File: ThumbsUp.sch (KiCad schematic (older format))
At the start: 159 parts, among them J19 52559-1233, J32 Battery, SW1 SW_Push, SW2 SW_DIP_x01, U1 ProMicro

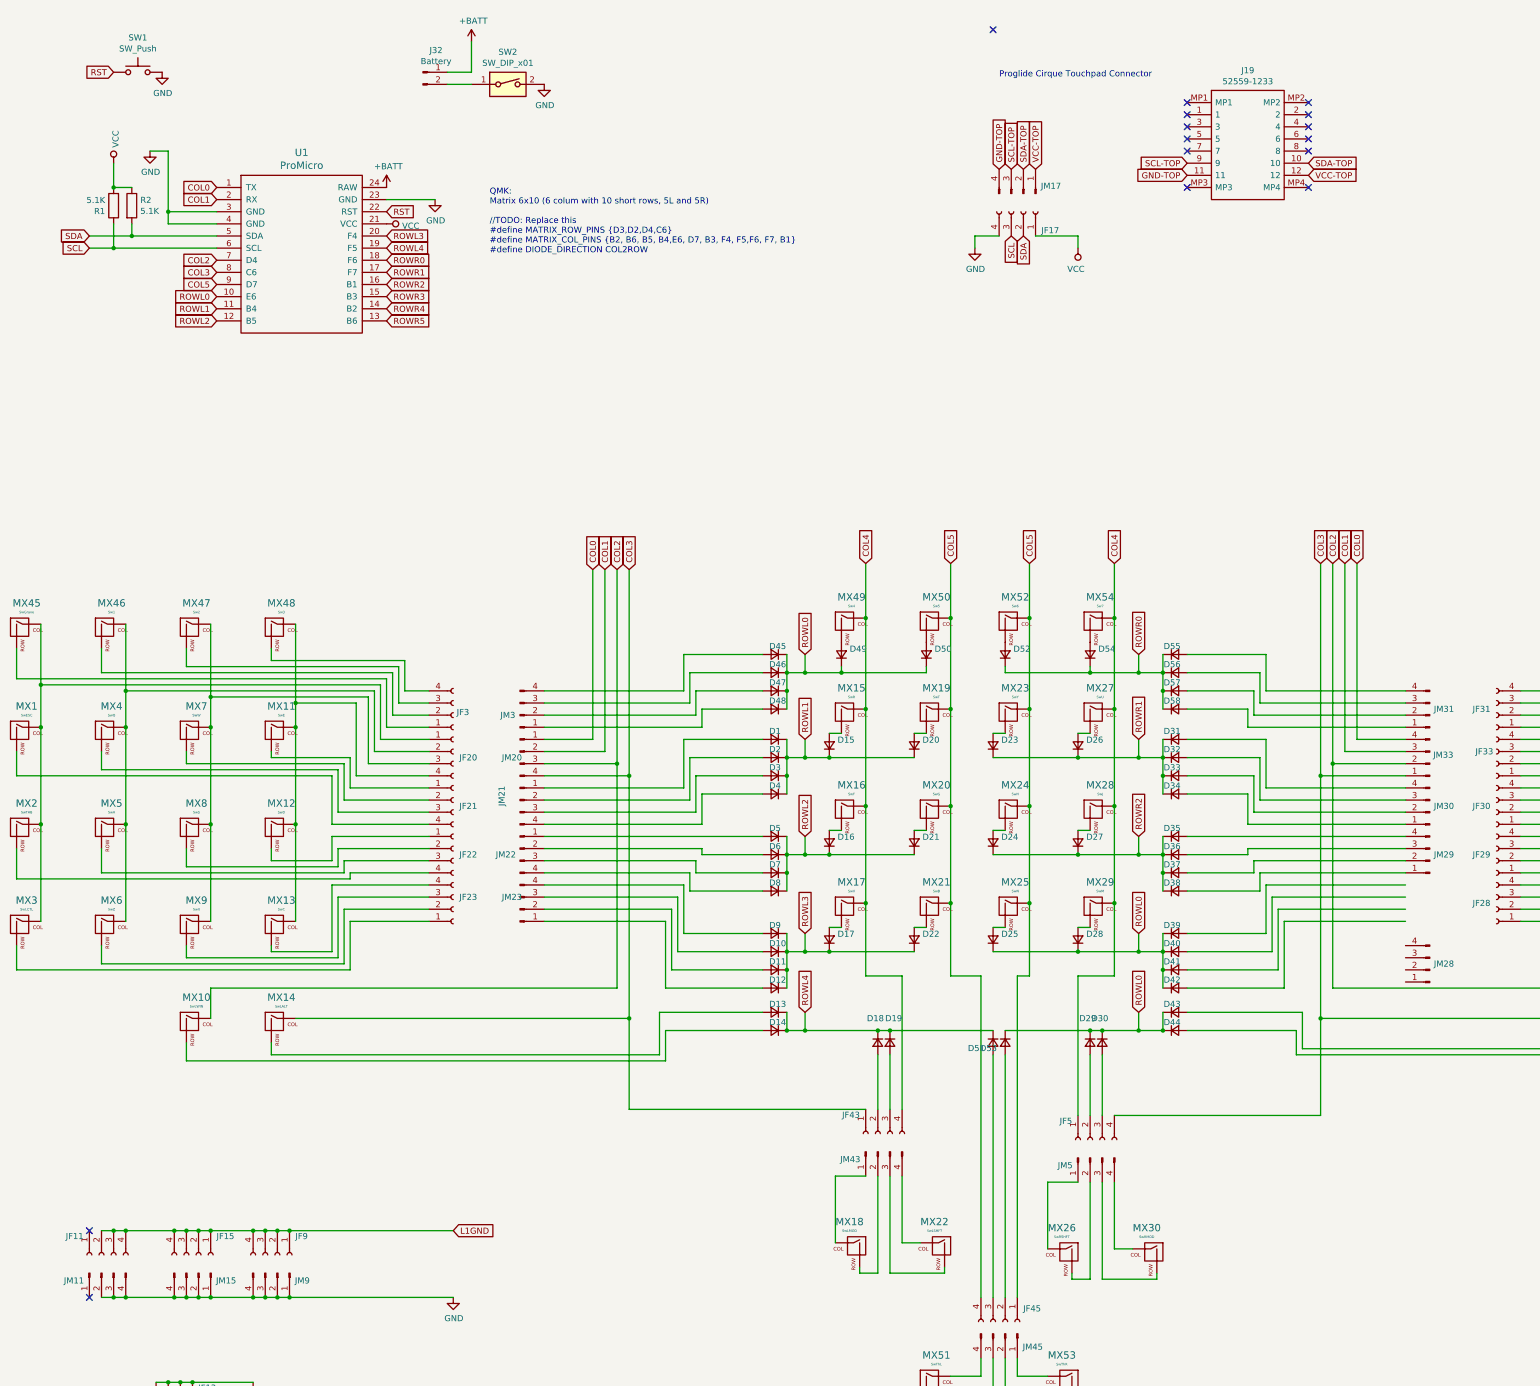
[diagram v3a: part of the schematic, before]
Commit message: Routed L2 PCB
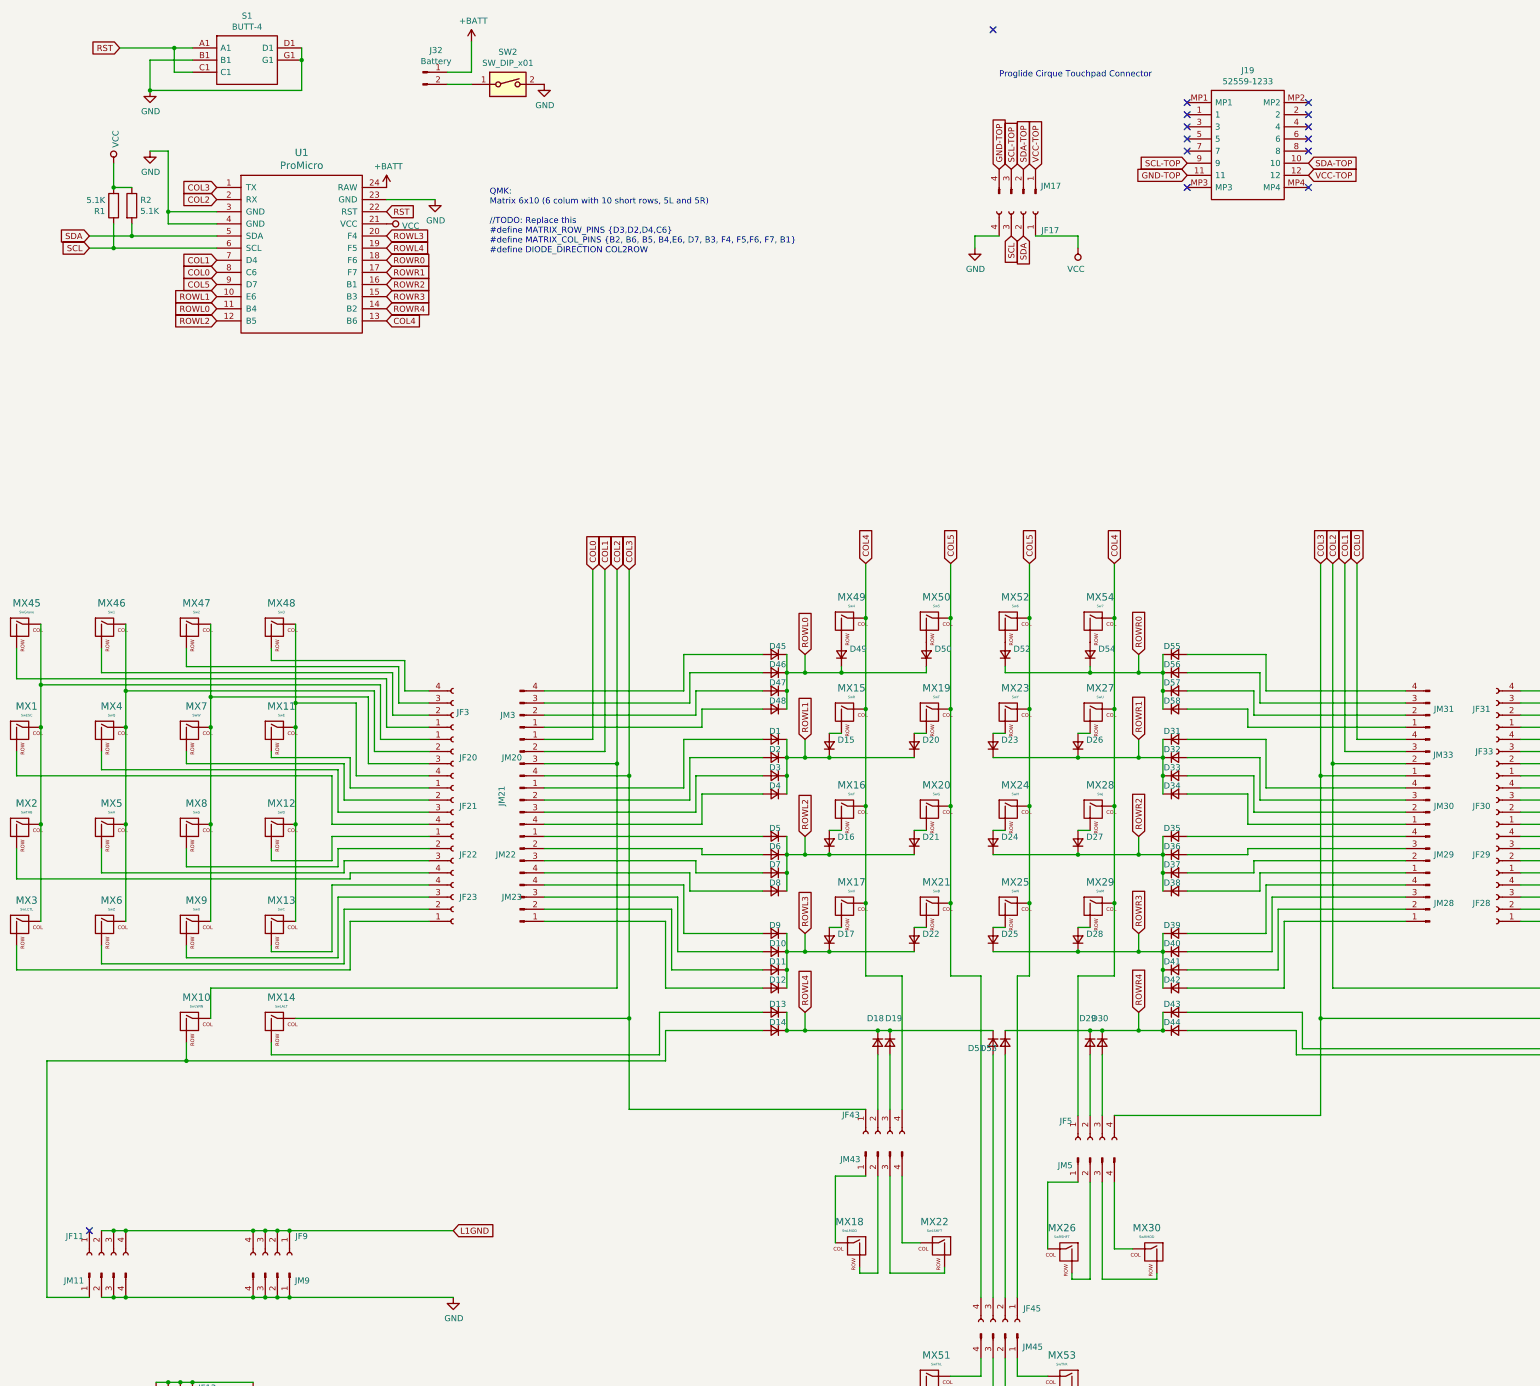
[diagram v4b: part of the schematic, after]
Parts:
- removed JF15: Raiser_Female, Connector_PinSocket_2.54mm:PinSocket_1x04_P2.54mm_Vertical, symbol Connector:Conn_01x04_Female
- removed JM15: Raiser_Male, Connector_PinHeader_2.54mm:PinHeader_1x04_P2.54mm_Vertical, symbol Connector:Conn_01x04_Male
- removed SW1: SW_Push, random-keyboard-parts:SKQG-1155865, symbol Switch:SW_Push
- added S1: BUTT-4, BUTT-4:BUTT4, symbol BUTT-4:BUTT-4
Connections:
- net ROWR5 is gone; now on net COL4: U1.13 (B6)
- net COL0: now also U1.8 (C6); no longer U1.1 (TX)
- net COL1: now also U1.7 (D4); no longer U1.2 (RX)
- net COL2: now also U1.2 (RX); no longer U1.7 (D4)
- net COL3: now also U1.1 (TX); no longer U1.8 (C6)
- net GND: now also S1.B1, S1.D1, S1.G1
- net ROWL0: now also U1.11 (B4); no longer D25.1 (K), D28.1 (K), D29.1 (K), D30.1 (K), D39.1 (K), D40.1 (K), D41.1 (K), D42.1 (K), D43.1 (K), D44.1 (K), D53.1 (K), U1.10 (E6)
- net ROWL1: now also U1.10 (E6); no longer U1.11 (B4)
- net ROWR3: now also D25.1 (K), D28.1 (K), D39.1 (K), D40.1 (K), D41.1 (K), D42.1 (K)
- net ROWR4: now also D29.1 (K), D30.1 (K), D43.1 (K), D44.1 (K), D53.1 (K)
- net RST: now also S1.A1, S1.C1
- net at D14.2 (A), MX10.2 (ROW): now also JM11.1 (Pin_1)
- net at D39.2 (A): now also JM28.4 (Pin_4)
- net at D40.2 (A): now also JM28.3 (Pin_3)
- net at D41.2 (A): now also JM28.2 (Pin_2)
- net at D42.2 (A): now also JM28.1 (Pin_1)
- no-connect marks 15 -> 14
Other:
- moved on the sheet: JM28
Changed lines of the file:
@@
-$EndComp
-$Comp
-L Connector:Conn_01x04_Female JF15
-U 1 1 6225ECEC
-P 2750 11050
-F 0 "JF15" V 2596 11198 50  0000 L CNN
-F 1 "Raiser_Female" V 2687 11198 50  0001 L CNN
-F 2 "Connector_PinSocket_2.54mm:PinSocket_1x04_P2.54mm_Vertical" H 2750 11050 50  0001 C CNN
-F 3 "~" H 2750 11050 50  0001 C CNN
-	1    2750 11050
-	0    1    1    0
-$EndComp
-$Comp
-L Connector:Conn_01x04_Male JM15
-U 1 1 6225ECF6
-P 2750 11200
-F 0 "JM15" V 2812 11344 50  0000 L CNN
-F 1 "Raiser_Male" V 2903 11344 50  0001 L CNN
-F 2 "Connector_PinHeader_2.54mm:PinHeader_1x04_P2.54mm_Vertical" H 2750 11200 50  0001 C CNN
-F 3 "~" H 2750 11200 50  0001 C CNN
-	1    2750 11200
-	0    1    1    0
 $EndComp
 $Comp
@@
 Text GLabel 1850 2750 0    50   Input ~ 0
 SCL
+Text GLabel 2900 2950 0    50   Input ~ 0
+COL0
+Text GLabel 2900 2850 0    50   Input ~ 0
+COL1
+Text GLabel 2900 2350 0    50   Input ~ 0
+COL2
 Text GLabel 2900 2250 0    50   Input ~ 0
-COL0
-Text GLabel 2900 2350 0    50   Input ~ 0
-COL1
-Text GLabel 2900 2850 0    50   Input ~ 0
-COL2
-Text GLabel 2900 2950 0    50   Input ~ 0
 COL3
 Text GLabel 2900 3050 0    50   Input ~ 0
 COL5
+Text GLabel 2900 3250 0    50   Input ~ 0
+ROWL0
 Text GLabel 2900 3150 0    50   Input ~ 0
-ROWL0
-Text GLabel 2900 3250 0    50   Input ~ 0
 ROWL1
 Text GLabel 2900 3350 0    50   Input ~ 0
@@
 Text GLabel 4300 3050 2    50   Input ~ 0
 ROWR2
-Text GLabel 4300 2950 2    50   Input ~ 0
-ROWR1
-Text GLabel 4300 2850 2    50   Input ~ 0
-ROWR0
 Text GLabel 4300 2750 2    50   Input ~ 0
 ROWL4
@@
 Text GLabel 4300 2450 2    50   Input ~ 0
 RST
-$Comp
-L Switch:SW_Push SW1
-U 1 1 63887BED
-P 2250 1300
-F 0 "SW1" H 2250 1585 50  0000 C CNN
-F 1 "SW_Push" H 2250 1494 50  0000 C CNN
-F 2 "random-keyboard-parts:SKQG-1155865" H 2250 1500 50  0001 C CNN
-F 3 "~" H 2250 1500 50  0001 C CNN
-	1    2250 1300
-	1    0    0    -1
-$EndComp
-Text GLabel 2050 1300 0    50   Input ~ 0
+Text GLabel 2100 1100 0    50   Input ~ 0
 RST
 $Comp
 L power:GND #PWR0104
 U 1 1 6388A683
-P 2450 1300
-F 0 "#PWR0104" H 2450 1050 50  0001 C CNN
-F 1 "GND" H 2455 1127 50  0000 C CNN
-F 2 "" H 2450 1300 50  0001 C CNN
-F 3 "" H 2450 1300 50  0001 C CNN
-	1    2450 1300
+P 2350 1450
+F 0 "#PWR0104" H 2350 1200 50  0001 C CNN
+F 1 "GND" H 2355 1277 50  0000 C CNN
+F 2 "" H 2350 1450 50  0001 C CNN
+F 3 "" H 2350 1450 50  0001 C CNN
+	1    2350 1450
 	1    0    0    -1
 $EndComp
@@
 $EndComp
 Text GLabel 10500 9050 1    50   Input ~ 0
-ROWL0
+ROWR4
 Text GLabel 10500 8400 1    50   Input ~ 0
-ROWL0
+ROWR3
 Wire Wire Line
 	9400 9400 9400 11400
@@
 Text GLabel 4300 3250 2    50   Input ~ 0
 ROWR4
-Text GLabel 4300 3350 2    50   Input ~ 0
-ROWR5
 Text GLabel 4300 3150 2    50   Input ~ 0
 ROWR3
@@
 	0    1    1    0
 $EndComp
-Connection ~ 2550 10850
-Wire Wire Line
-	2550 10850 2650 10850
-Connection ~ 2650 10850
-Wire Wire Line
-	2650 10850 2750 10850
-Connection ~ 2750 10850
-Wire Wire Line
-	2750 10850 2850 10850
-Connection ~ 2850 10850
-Wire Wire Line
-	2850 10850 3200 10850
 Connection ~ 3200 10850
 Wire Wire Line
@@
 	3400 10850 3500 10850
 Connection ~ 3500 10850
-Connection ~ 2550 11400
-Wire Wire Line
-	2550 11400 2650 11400
-Connection ~ 2650 11400
-Wire Wire Line
-	2650 11400 2750 11400
-Connection ~ 2750 11400
-Wire Wire Line
-	2750 11400 2850 11400
-Connection ~ 2850 11400
-Wire Wire Line
-	2850 11400 3200 11400
 Connection ~ 3200 11400
 Wire Wire Line
@@
 	9650 2650 10000 2650
 Wire Wire Line
-	2150 10850 2550 10850
-Wire Wire Line
 	1950 10850 2050 10850
 Connection ~ 2150 10850
@@
 NoConn ~ 1850 10850
 Wire Wire Line
-	2150 11400 2550 11400
-Wire Wire Line
 	2150 11400 2050 11400
 Connection ~ 2150 11400
@@
 Wire Wire Line
 	2050 11400 1950 11400
-NoConn ~ 1850 11400
 $Comp
 L Connector:Conn_01x04_Female JF31
@@
 L Connector:Conn_01x04_Male JM28
 U 1 1 636DA3EC
-P 12900 8700
-F 0 "JM28" H 12700 8650 50  0000 L CNN
-F 1 "Conn_01x04_Male" H 13053 8844 50  0001 L CNN
-F 2 "Connector_PinHeader_2.54mm:PinHeader_1x04_P2.54mm_Vertical" H 12900 8700 50  0001 C CNN
-F 3 "~" H 12900 8700 50  0001 C CNN
-	1    12900 8700
+P 12900 8200
+F 0 "JM28" H 12700 8150 50  0000 L CNN
+F 1 "Conn_01x04_Male" H 13053 8344 50  0001 L CNN
+F 2 "Connector_PinHeader_2.54mm:PinHeader_1x04_P2.54mm_Vertical" H 12900 8200 50  0001 C CNN
+F 3 "~" H 12900 8200 50  0001 C CNN
+	1    12900 8200
 	-1   0    0    1
 $EndComp
@@
 L1GND
 $Comp
-L power:GND #PWR?
+L power:GND #PWR0112
 U 1 1 6569DA14
 P 3200 12100
-F 0 "#PWR?" H 3200 11850 50  0001 C CNN
+F 0 "#PWR0112" H 3200 11850 50  0001 C CNN
 F 1 "GND" H 3205 11927 50  0000 C CNN
 F 2 "" H 3200 12100 50  0001 C CNN
@@
 Wire Wire Line
 	2700 12600 3200 12600
+$Comp
+L BUTT-4:BUTT-4 S1
+U 1 1 646FD412
+P 2700 1100
+F 0 "S1" H 3150 1365 50  0000 C CNN
+F 1 "BUTT-4" H 3150 1274 50  0000 C CNN
+F 2 "BUTT-4:BUTT4" H 3450 1200 50  0001 L CNN
+F 3 "http://site.gravitech.us/Components/BUTT-4/BUTT-4_datasheet.pdf" H 3450 1100 50  0001 L CNN
+F 4 "Tactile Switches MINI PUSH BUTTON SWITCH 4-PIN QTY. 4" H 3450 1000 50  0001 L CNN "Description"
+F 5 "9.5" H 3450 900 50  0001 L CNN "Height"
+F 6 "Gravitech" H 3450 800 50  0001 L CNN "Manufacturer_Name"
+F 7 "BUTT-4" H 3450 700 50  0001 L CNN "Manufacturer_Part_Number"
+F 8 "992-BUTT-4" H 3450 600 50  0001 L CNN "Mouser Part Number"
+F 9 "https://www.mouser.co.uk/ProductDetail/Gravitech/BUTT-4?qs=Vxac6xGyzPm51iLpy8GNew%3D%3D" H 3450 500 50  0001 L CNN "Mouser Price/Stock"
+F 10 "" H 3450 400 50  0001 L CNN "Arrow Part Number"
+F 11 "" H 3450 300 50  0001 L CNN "Arrow Price/Stock"
+	1    2700 1100
+	1    0    0    -1
+$EndComp
+Wire Wire Line
+	2100 1100 2550 1100
+Wire Wire Line
+	2700 1200 2350 1200
+Wire Wire Line
+	2350 1200 2350 1450
+Wire Wire Line
+	2700 1300 2550 1300
+Wire Wire Line
+	2550 1300 2550 1100
+Connection ~ 2550 1100
+Wire Wire Line
+	2550 1100 2700 1100
+Wire Wire Line
+	2350 1450 3600 1450
+Wire Wire Line
+	3600 1450 3600 1200
+Connection ~ 2350 1450
+Connection ~ 3600 1200
+Wire Wire Line
+	3600 1200 3600 1100
+Wire Wire Line
+	1850 11400 1500 11400
+Wire Wire Line
+	1500 11400 1500 9450
+Wire Wire Line
+	1500 9450 2650 9450
+Connection ~ 2650 9450
+Text GLabel 4300 2850 2    50   Input ~ 0
+ROWR0
+Text GLabel 4300 2950 2    50   Input ~ 0
+ROWR1
+Text GLabel 4300 3350 2    50   Input ~ 0
+COL4
+Wire Wire Line
+	2150 11400 3200 11400
+Wire Wire Line
+	2150 10850 3200 10850
 $EndSCHEMATC

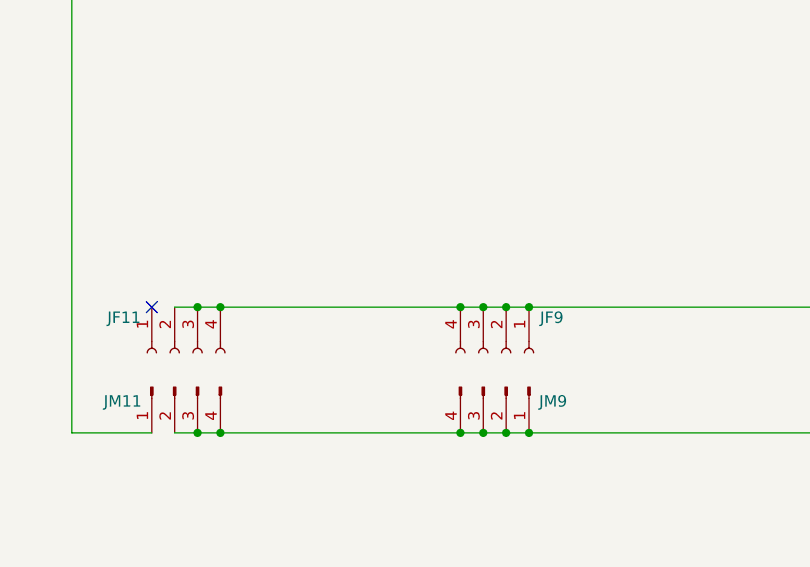
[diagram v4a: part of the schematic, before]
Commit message: Added mounting holes, enlarged ProMicro pin holes to fit machined sockets.
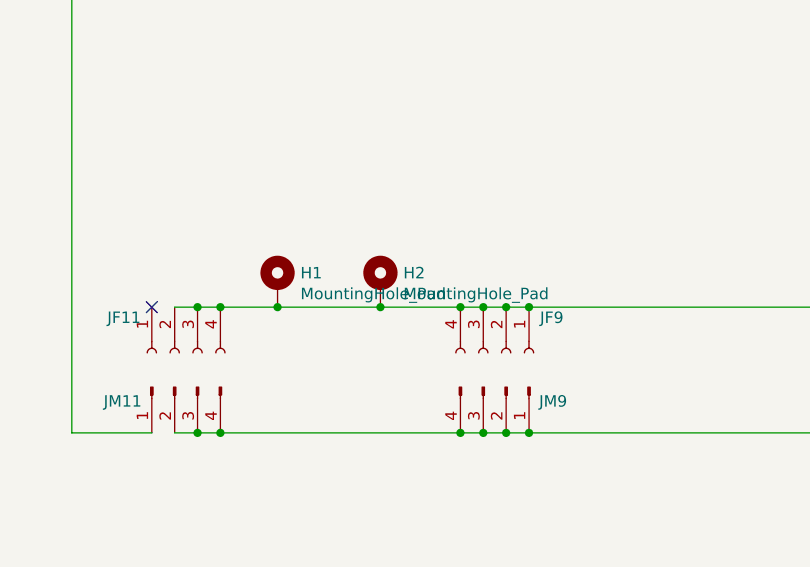
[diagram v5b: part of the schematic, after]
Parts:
- added H1: MountingHole_Pad, MountingHole:MountingHole_6mm_Pad_Via, symbol Mechanical:MountingHole_Pad
- added H2: MountingHole_Pad, MountingHole:MountingHole_8.4mm_M8_Pad_Via, symbol Mechanical:MountingHole_Pad
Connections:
- net L1GND: now also H1.1, H2.1
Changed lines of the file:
@@
 	2150 11400 3200 11400
 Wire Wire Line
-	2150 10850 3200 10850
+	2150 10850 2400 10850
+$Comp
+L Mechanical:MountingHole_Pad H1
+U 1 1 6471D2FA
+P 2400 10750
+F 0 "H1" H 2500 10799 50  0000 L CNN
+F 1 "MountingHole_Pad" H 2500 10708 50  0000 L CNN
+F 2 "MountingHole:MountingHole_6mm_Pad_Via" H 2400 10750 50  0001 C CNN
+F 3 "~" H 2400 10750 50  0001 C CNN
+	1    2400 10750
+	1    0    0    -1
+$EndComp
+Connection ~ 2400 10850
+Wire Wire Line
+	2400 10850 2850 10850
+$Comp
+L Mechanical:MountingHole_Pad H2
+U 1 1 6471E1B6
+P 2850 10750
+F 0 "H2" H 2950 10799 50  0000 L CNN
+F 1 "MountingHole_Pad" H 2950 10708 50  0000 L CNN
+F 2 "MountingHole:MountingHole_8.4mm_M8_Pad_Via" H 2850 10750 50  0001 C CNN
+F 3 "~" H 2850 10750 50  0001 C CNN
+	1    2850 10750
+	1    0    0    -1
+$EndComp
+Connection ~ 2850 10850
+Wire Wire Line
+	2850 10850 3200 10850
 $EndSCHEMATC
